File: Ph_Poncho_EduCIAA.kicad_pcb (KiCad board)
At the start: 2 copper layers, 41.3 x 60.8 mm, 34 parts, among them P1 BNC, U1 LMC7660, U2 CA3140, U3 TL081

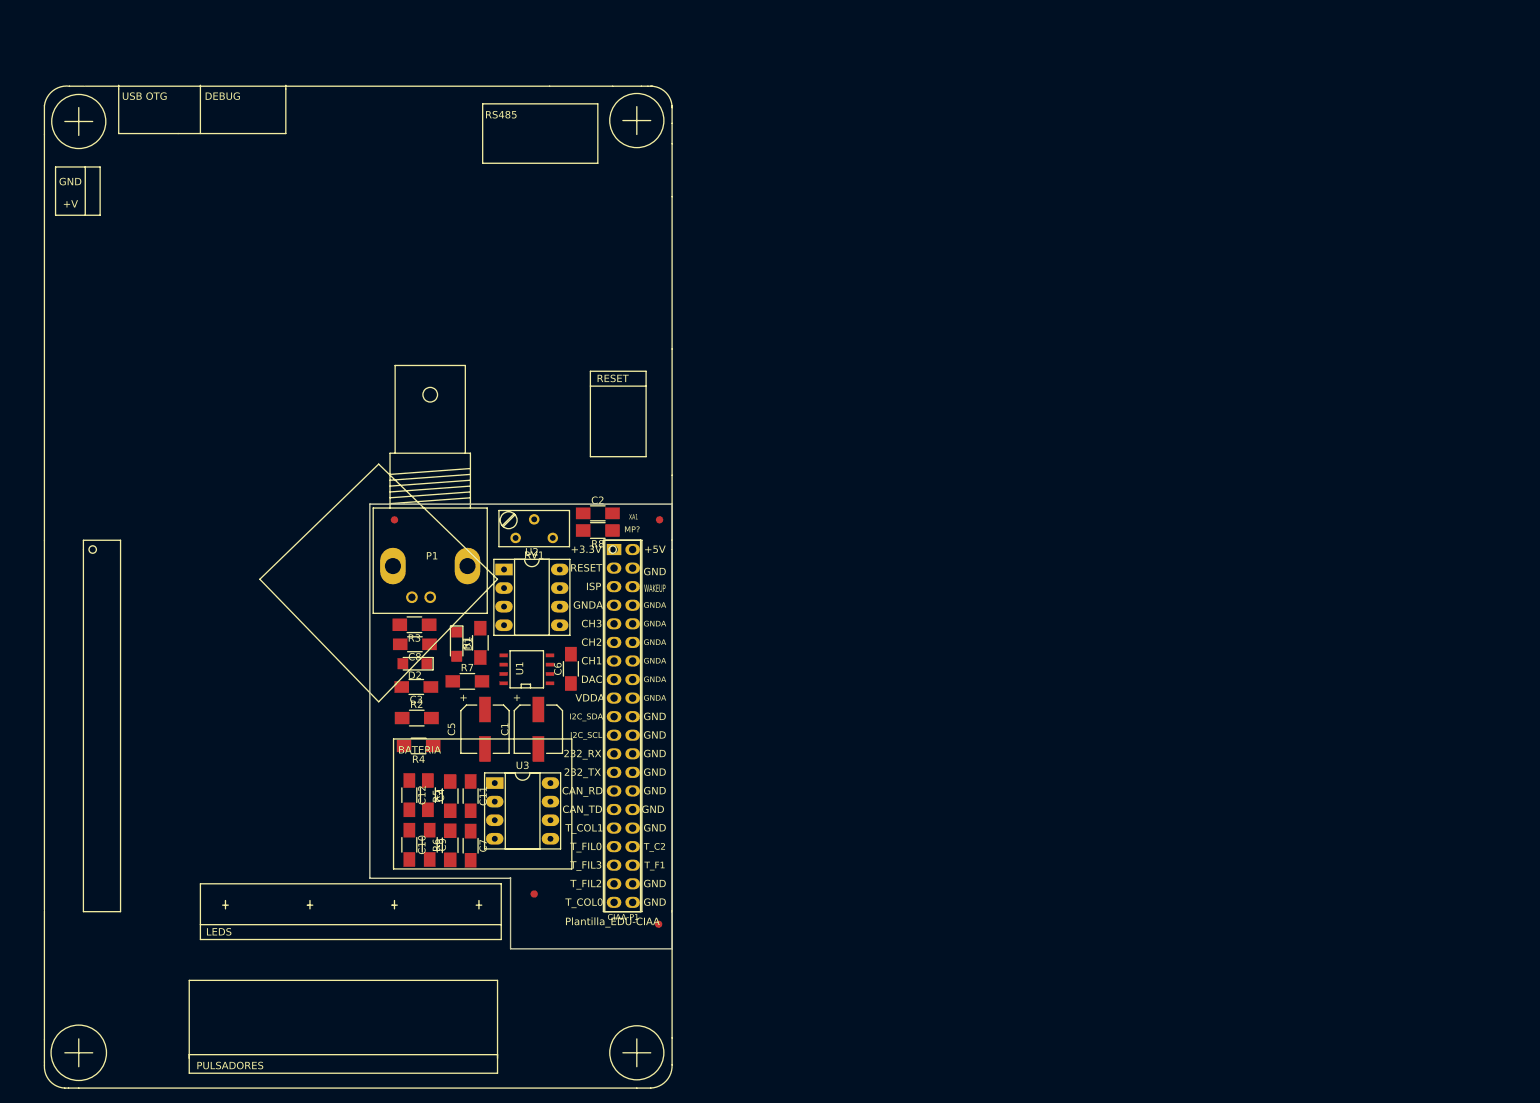
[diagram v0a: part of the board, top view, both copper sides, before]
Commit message: Agregando el ruteo del PCB
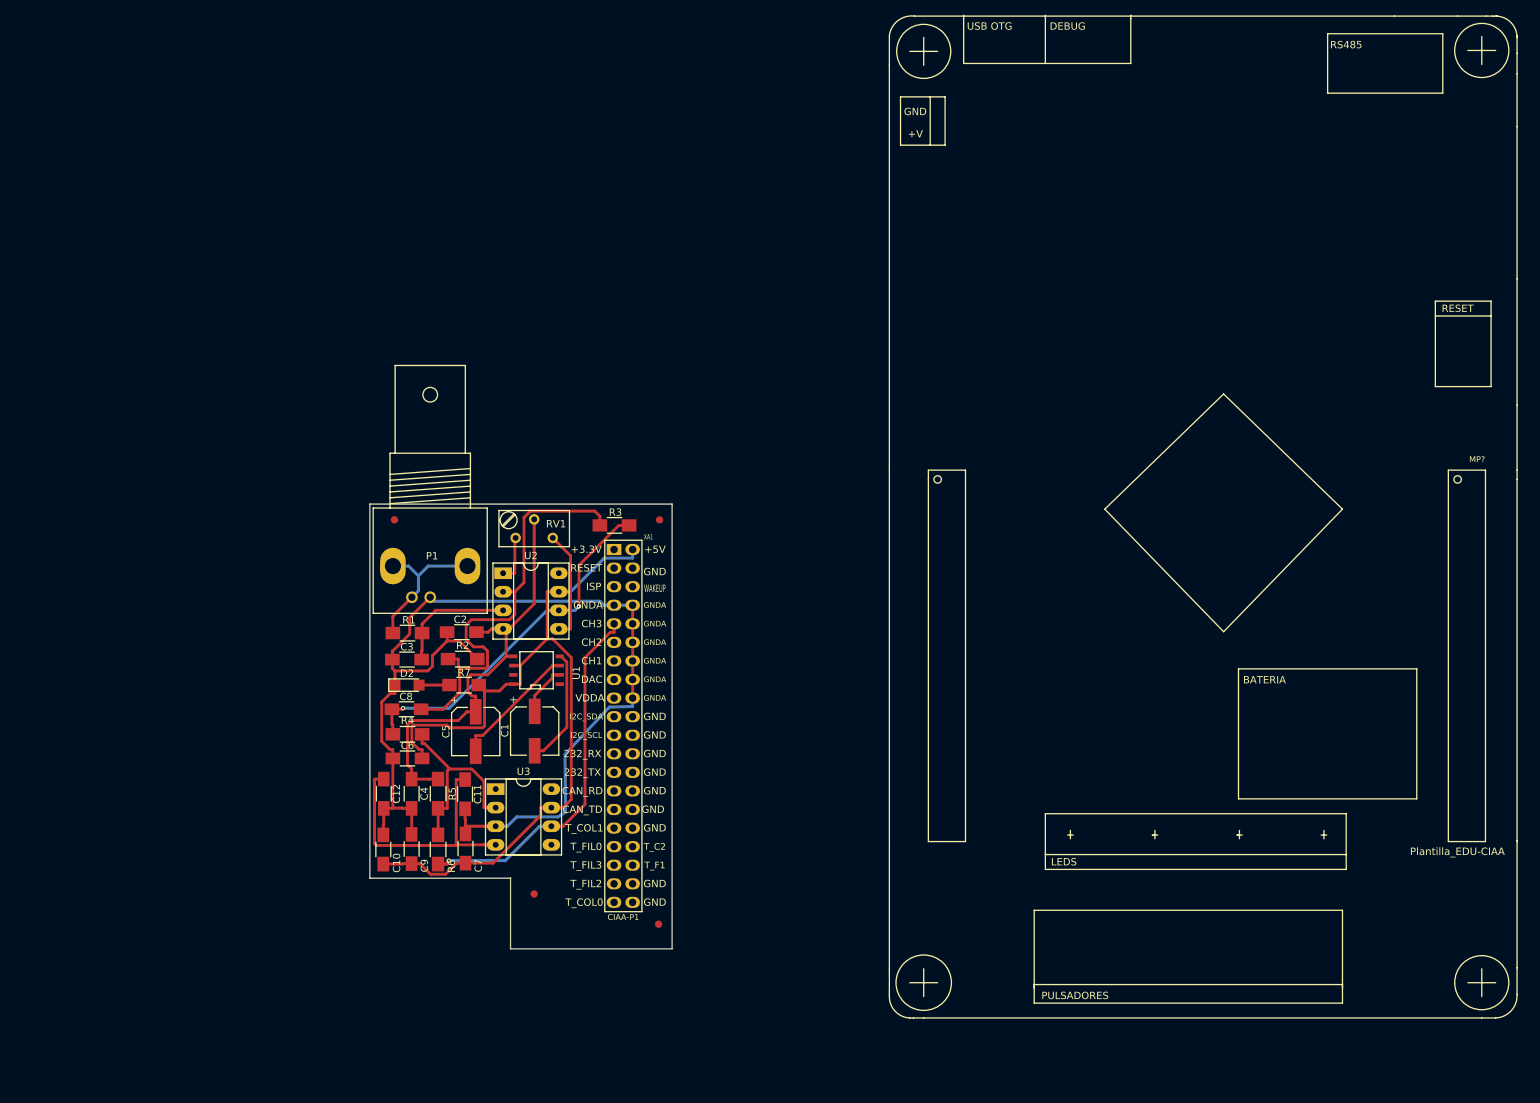
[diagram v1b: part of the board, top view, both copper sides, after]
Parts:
- removed D1: Led_Small, Ph_Poncho:LED_1206
- removed R8: 1K, Ph_Poncho:R_1206_HandSoldering
- moved MP? 116.0 mm to (372.8, 38.9)
- moved R3 30.6 mm to (257.5, 45.2)
- moved C6 25.5 mm to (229.2, 77.1), turned to 0 degrees
- moved C2 24.7 mm to (236.6, 59.8), turned to 180 degrees
- moved R2 10.2 mm to (236.7, 63.5)
- moved R1 10.1 mm to (229.2, 59.9), turned to 180 degrees
- moved C8 8.96 mm to (229.0, 70.4), turned to 0 degrees
- moved C3 3.96 mm to (229.1, 63.6)
- moved C10 3.61 mm to (225.9, 89.5)
- moved C12 3.50 mm to (225.9, 81.9)
- moved D2 3.11 mm to (229.1, 67.1), turned to 0 degrees
- moved C9 2.54 mm to (229.7, 89.5)
- moved C4 2.23 mm to (229.7, 81.9)
- moved R4 2.20 mm to (229.2, 73.8)
- moved R6 1.75 mm to (233.4, 89.5)
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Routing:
- net GNDA: track 0.00 -> 140.1 mm
- net +5V: track 0.00 -> 111.5 mm
- net VEE: track 0.00 -> 59.7 mm
- net Net-(C8-Pad2): track 0.00 -> 58.8 mm
- net /ADC3: track 0.00 -> 50.3 mm, vias 0 -> 1
- net Net-(C8-Pad1): track 0.00 -> 49.6 mm, vias 0 -> 2
- net Net-(C11-Pad1): track 0.00 -> 36.9 mm
- net Net-(R4-Pad1): track 0.00 -> 27.5 mm
- net Net-(P1-Pad2): track 0.00 -> 20.6 mm
- net GND: track 0.00 -> 17.6 mm
- net Net-(C3-Pad1): track 0.00 -> 16.7 mm
- net Net-(C1-Pad2): track 0.00 -> 16.0 mm
- net Net-(RV1-Pad3): track 0.00 -> 15.1 mm
- net Net-(C1-Pad1): track 0.00 -> 6.97 mm
- net Net-(RV1-Pad1): track 0.00 -> 6.47 mm
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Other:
- net class Default: trace_width 0.25 -> 0.4

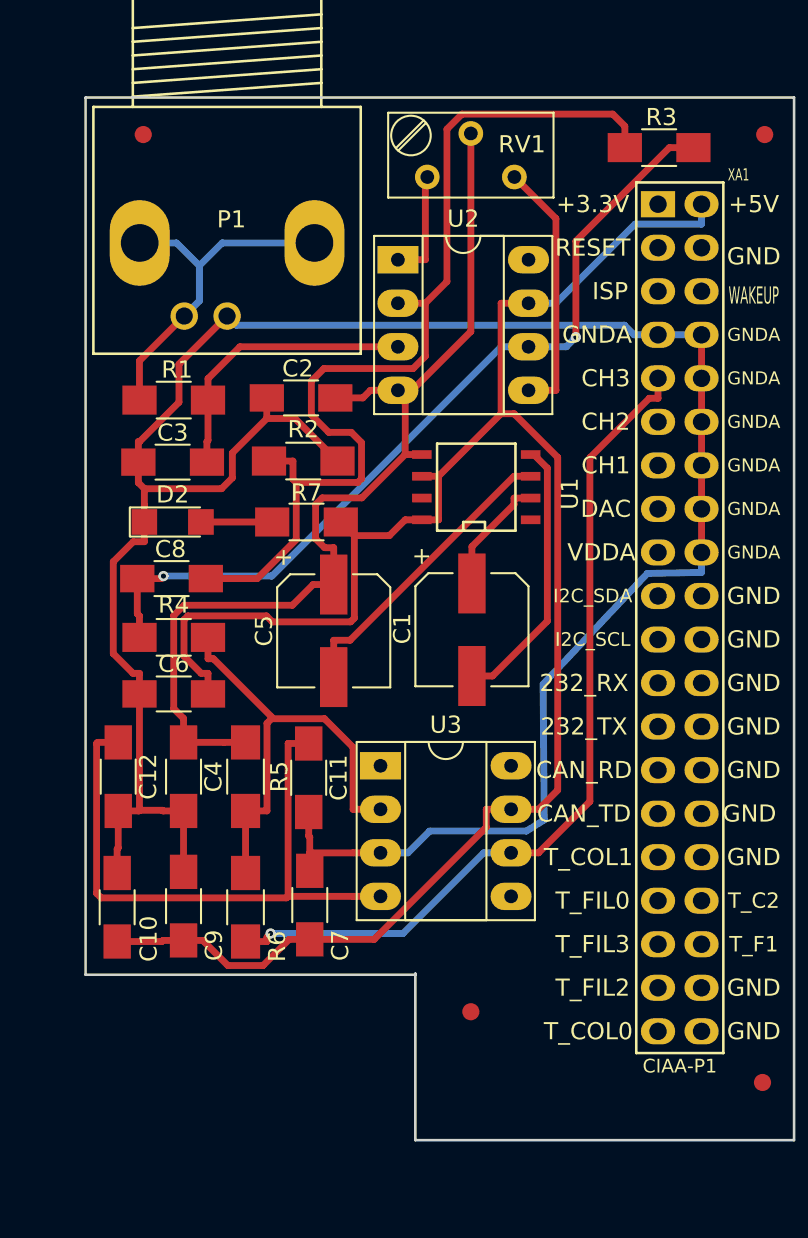
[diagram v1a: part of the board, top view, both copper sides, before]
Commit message: Modificación de pistas
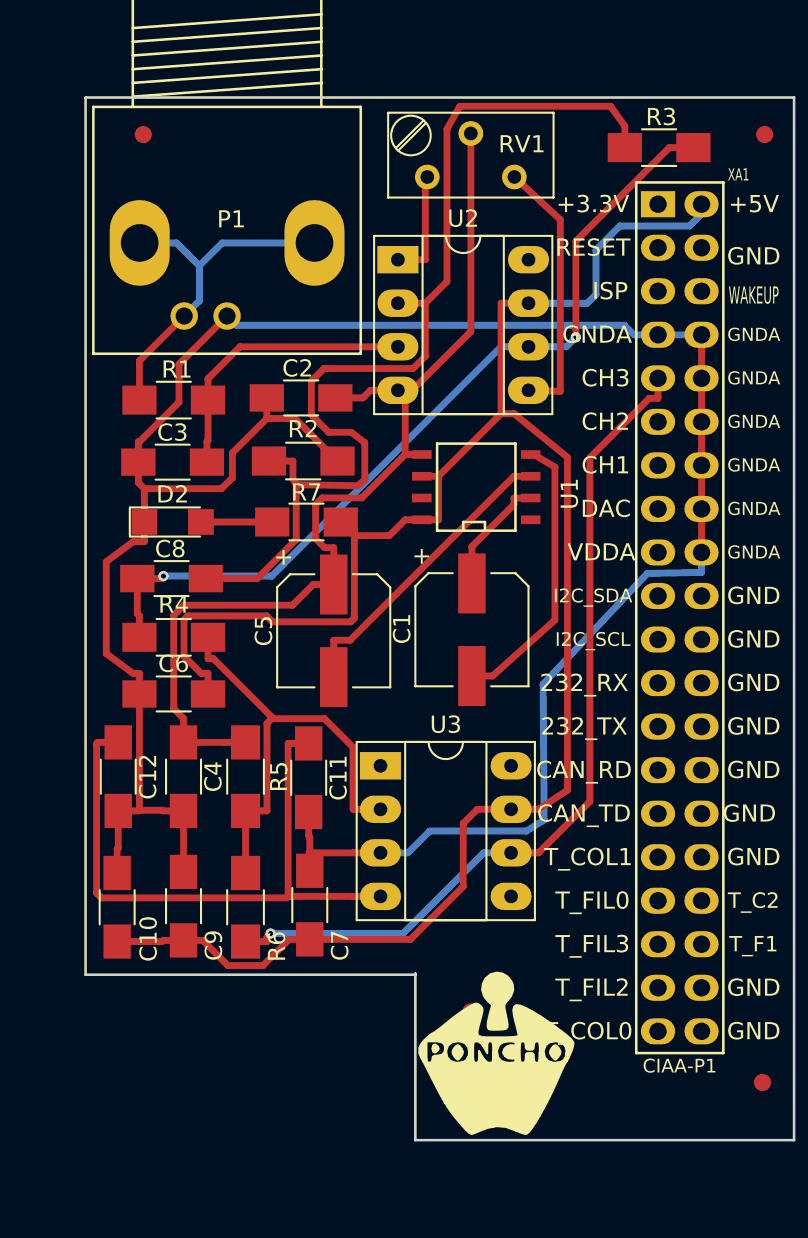
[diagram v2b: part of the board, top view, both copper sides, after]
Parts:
- added G***: LOGO, Ph_Poncho:Logo_Poncho, F.Cu at (248.0, 98.1)
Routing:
- net +5V: track 111.5 -> 115.1 mm
- net Net-(C8-Pad2): track 58.8 -> 59.9 mm
- net Net-(C1-Pad2): track 16.0 -> 16.6 mm
- net GNDA: track 140.1 -> 140.7 mm

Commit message: Subiendo modificaciones, correcciones y primera versión de la placa ruteada y con planos de tierra
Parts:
- added G***: Logo_EDU-CIAA, Ph_Poncho:Logo_EDU-CIAA, B.Cu at (234.5, 77.2)
- added G101: Logo_OSHWA, Ph_Poncho:Logo_OSHWA, B.Cu at (231.8, 63.6)
- U2, U3: footprint Ph_Poncho:DIP-8_W7.62mm_Socket_LongPads -> Ph_Poncho:SOIC-8-N
- moved MP? 115.9 mm to (257.3, 48.4)
- moved XA? 65.0 mm to (91.4, 26.5)
- moved F3 62.4 mm to (254.5, 100.6)
- moved R6 25.4 mm to (246.5, 67.8), turned to 180 degrees
- moved U1 23.5 mm to (236.5, 86.1)
- moved C7 21.7 mm to (236.1, 67.7), turned to 0 degrees
- moved C12 21.4 mm to (246.4, 75.6), turned to 0 degrees
- moved C8 21.4 mm to (246.6, 58.2), turned to 180 degrees
- moved U3 19.6 mm to (246.6, 62.5), turned to 270 degrees
- moved C5 17.0 mm to (227.5, 86.4)
- moved R5 16.5 mm to (246.4, 71.8), turned to 0 degrees
- moved C9 14.9 mm to (236.0, 75.9), turned to 0 degrees
- moved C10 14.1 mm to (236.0, 79.8), turned to 0 degrees
- moved C1 13.3 mm to (246.1, 86.6), turned to 90 degrees
- moved R7 11.5 mm to (226.6, 72.0)
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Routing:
- net VEE: track 59.7 -> 91.2 mm, vias 0 -> 2
- net /ADC3: track 50.3 -> 18.9 mm, vias 1 -> 3
- net Net-(C11-Pad1): track 36.9 -> 18.0 mm
- net Net-(C8-Pad2): track 59.9 -> 45.2 mm, vias 0 -> 4
- net +5V: track 115.1 -> 127.0 mm, vias 0 -> 4
- net Net-(C1-Pad2): track 16.6 -> 6.60 mm
- net Net-(C3-Pad1): track 16.7 -> 25.0 mm
- net GNDA: track 140.7 -> 132.7 mm, vias 0 -> 8
- net Net-(P1-Pad2): track 20.6 -> 25.5 mm
- net Net-(R4-Pad1): track 27.5 -> 22.7 mm, vias 0 -> 2
- net Net-(RV1-Pad3): track 15.5 -> 11.1 mm
- net GND: track 17.6 -> 20.9 mm, vias 0 -> 2
- net Net-(RV1-Pad1): track 6.47 -> 4.04 mm
- net Net-(C8-Pad1): track 49.6 -> 49.0 mm
- net Net-(C1-Pad1): track 6.97 -> 7.54 mm
- added copper zone on B.Cu, net /ADC3
- added copper zone on F.Cu, net VEE
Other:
- board size 41.3 x 60.8 mm -> 44.3 x 63.2 mm
- net class Default: clearance 0.2 -> 0.2794; trace_width 0.4 -> 0.3048; via_dia 0.6 -> 1.27; via_drill 0.4 -> 0.7112
- rule trace_clearance: 0.2 -> 0.2794
- rule trace_min: 0.2 -> 0.2794
- rule via_min_drill: 0.3 -> 0.7112
- rule via_min_size: 0.4 -> 1.27
- board text added: "1 Oz"
- board text added: "INDUSTRIA ARGENTINA"
- board text added: "L1 - TOP (VCC/VEE/SIGNAL)"
- board text added: "L2 - GND (Plane)"
- board text added: "Prepeg Isola 2 x 7628AT05"
- board text added: "Stack-Up"
